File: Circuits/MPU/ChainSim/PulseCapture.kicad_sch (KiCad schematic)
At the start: 24 parts, among them U7 LT1715, U8 ADA4805-2ARMZ, U9 AD7984BRMZ

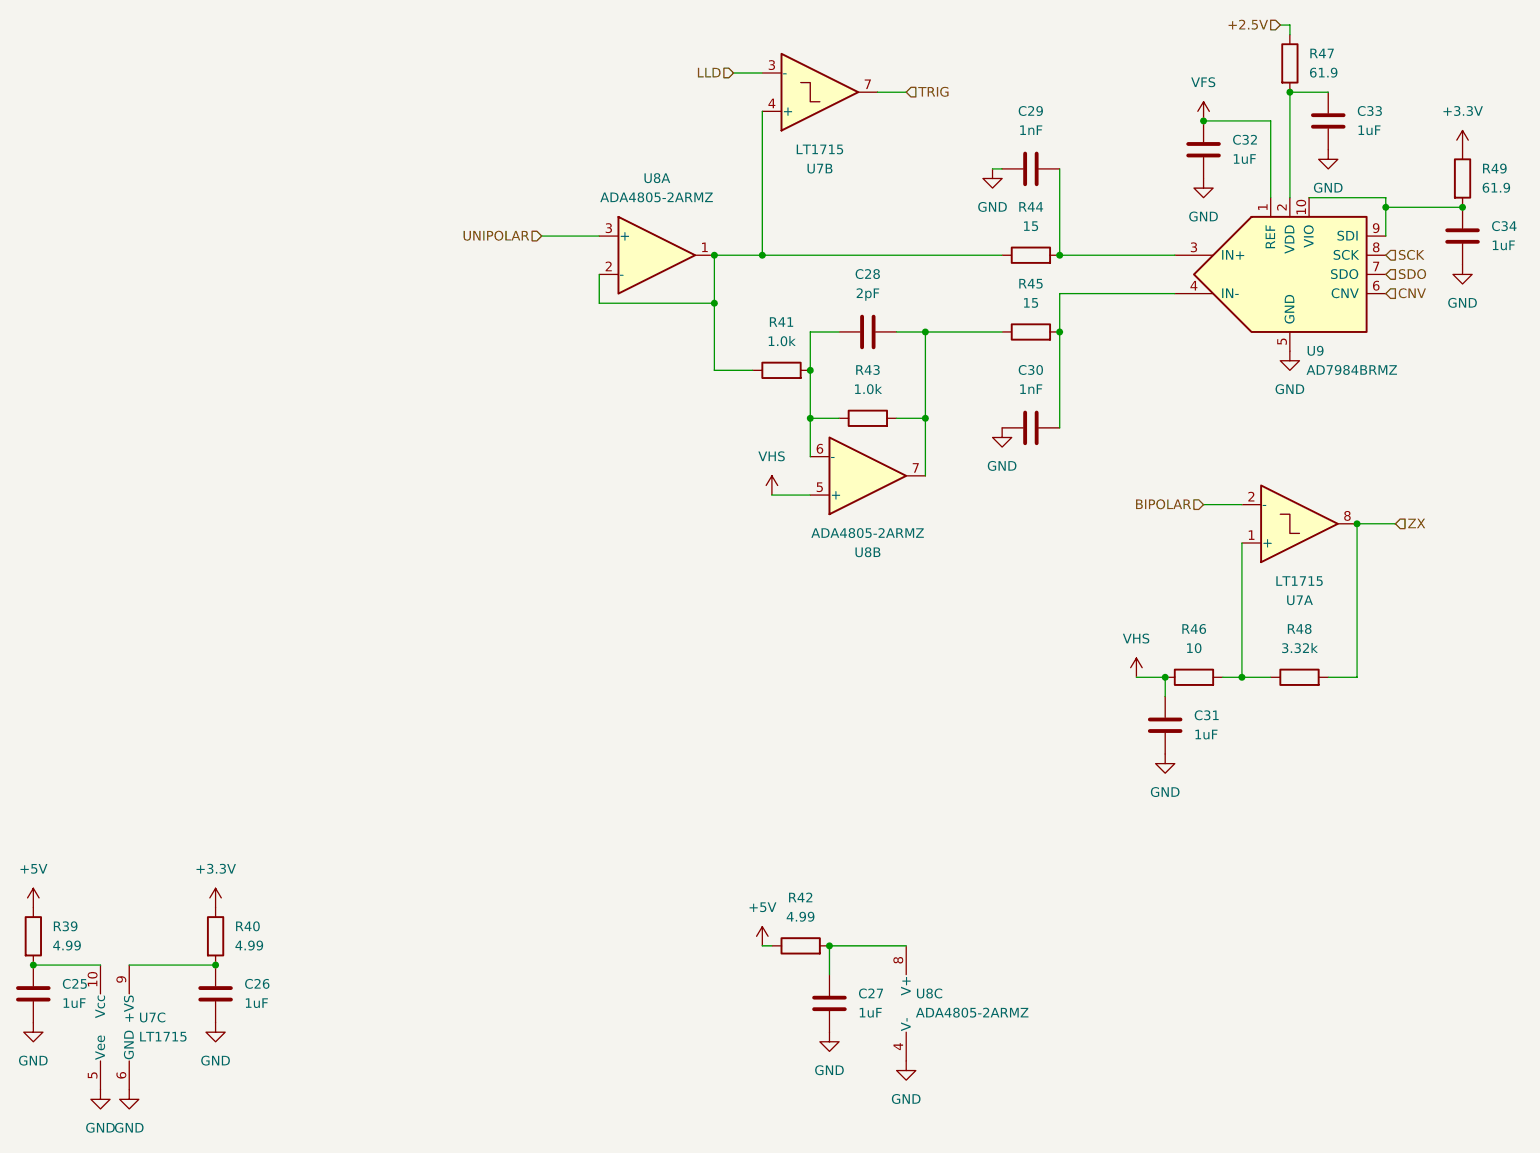
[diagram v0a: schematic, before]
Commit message: Chainsim working, a little tuneup
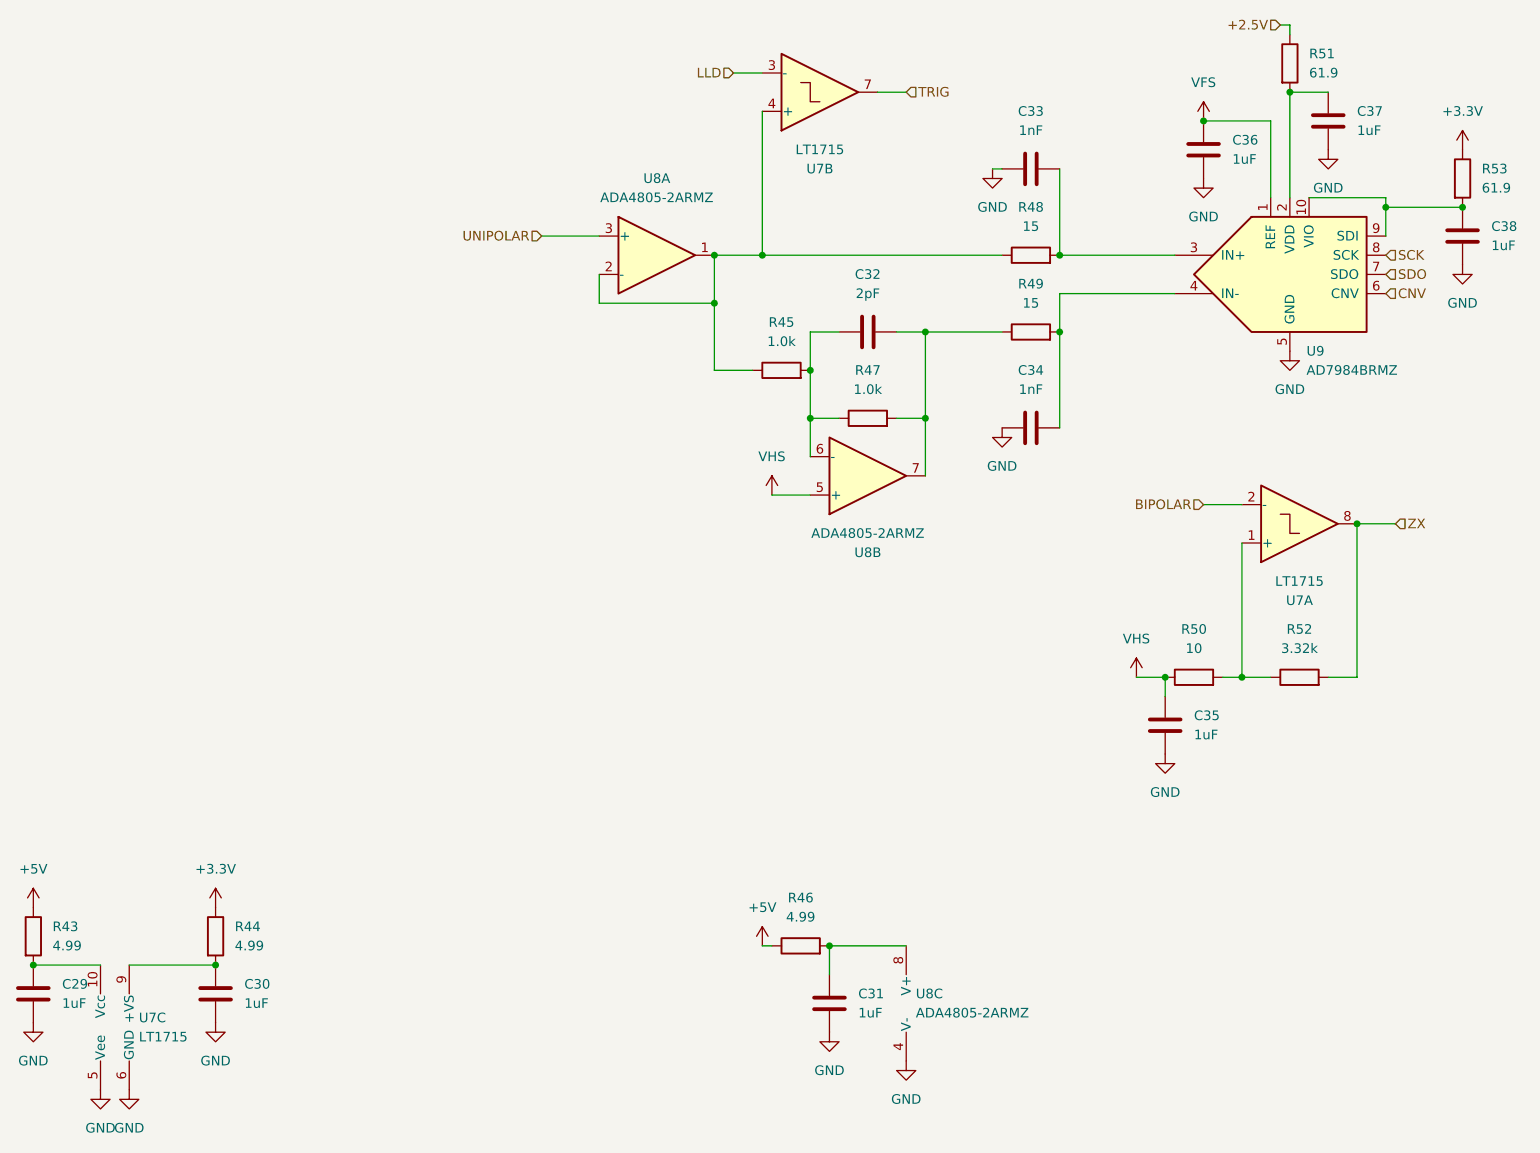
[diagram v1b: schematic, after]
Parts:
- renumbered C25 to C29, C26 to C30, C27 to C31, C28 to C32, C29 to C33, C30 to C34, C31 to C35, C32 to C36, C33 to C37, C34 to C38, R39 to R43, R40 to R44, R41 to R45, R42 to R46, R43 to R47, R44 to R48, R45 to R49, R46 to R50, R47 to R51, R48 to R52, R49 to R53
